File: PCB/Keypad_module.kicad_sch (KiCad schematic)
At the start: 67 parts, among them SW83 SW_Push, SW84 SW_Push, SW85 SW_Push, SW86 SW_Push, SW87 SW_Push, SW88 SW_Push, SW89 SW_Push, SW90 SW_Push, SW91 SW_Push, SW92 SW_Push, SW93 SW_Push, SW94 SW_Push, SW95 SW_Push, SW96 SW_Push, SW97 SW_Push, SW98 SW_Push, SW99 SW_Push, U5 XIAO-nRF52840-SMD, U6 MCP23017_ML

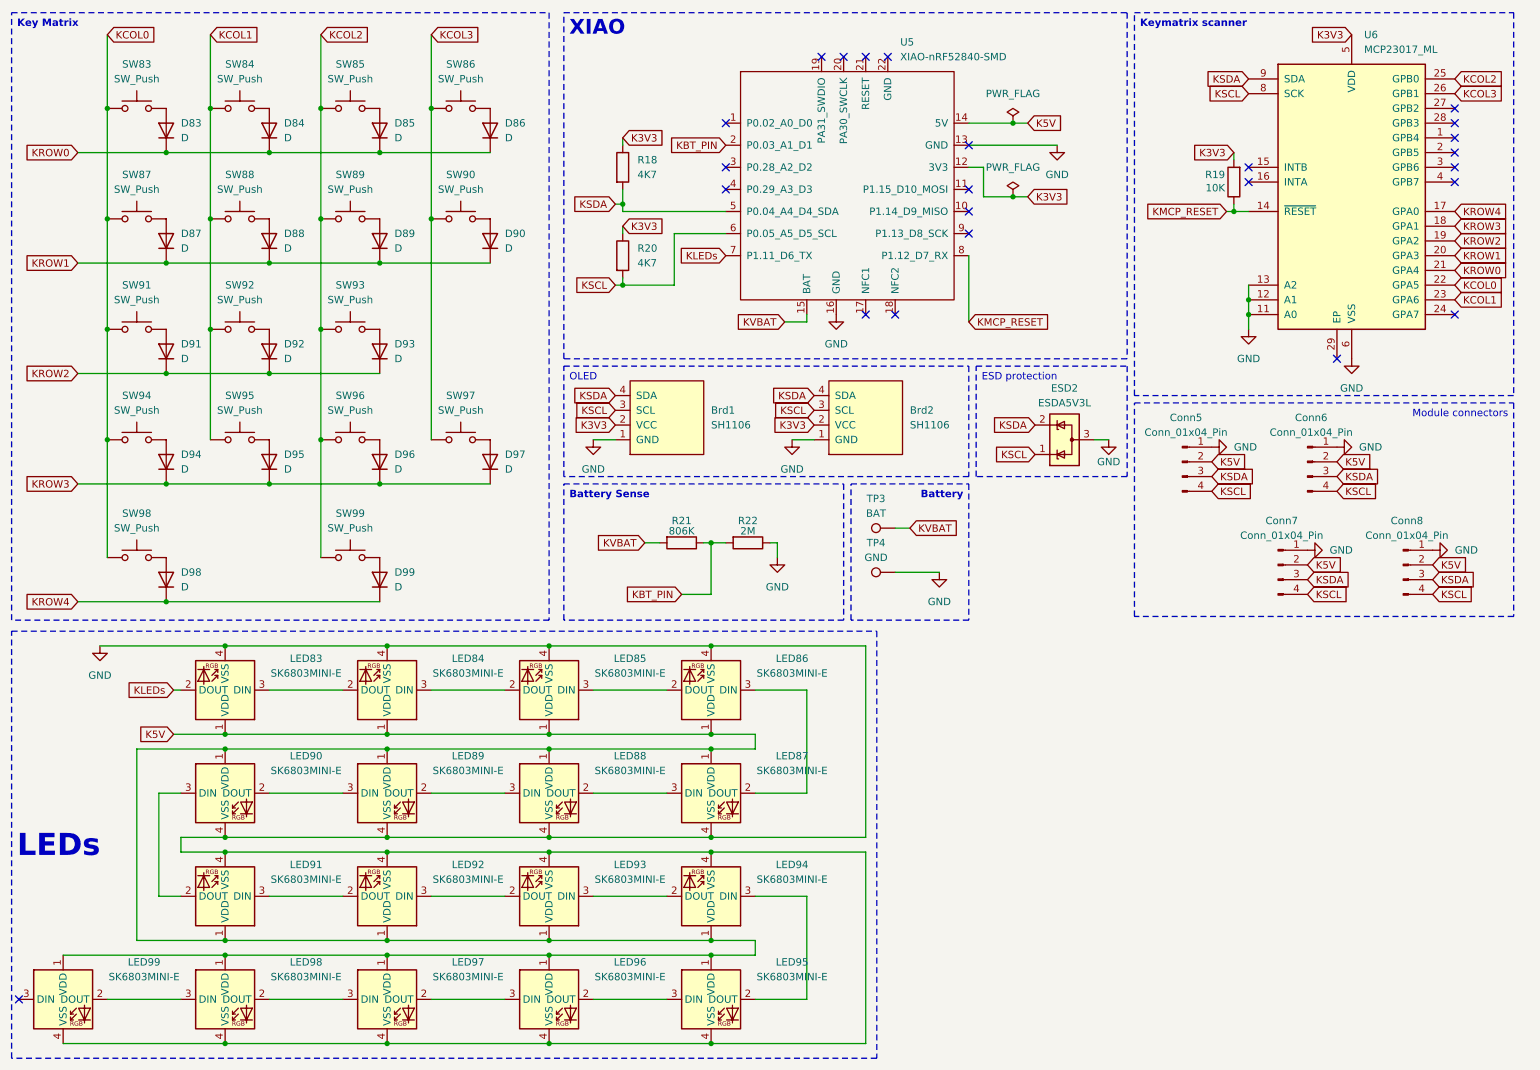
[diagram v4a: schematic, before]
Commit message: Update: schematic and PCB
Replaced the MT3608 module with a custom circuit for it.
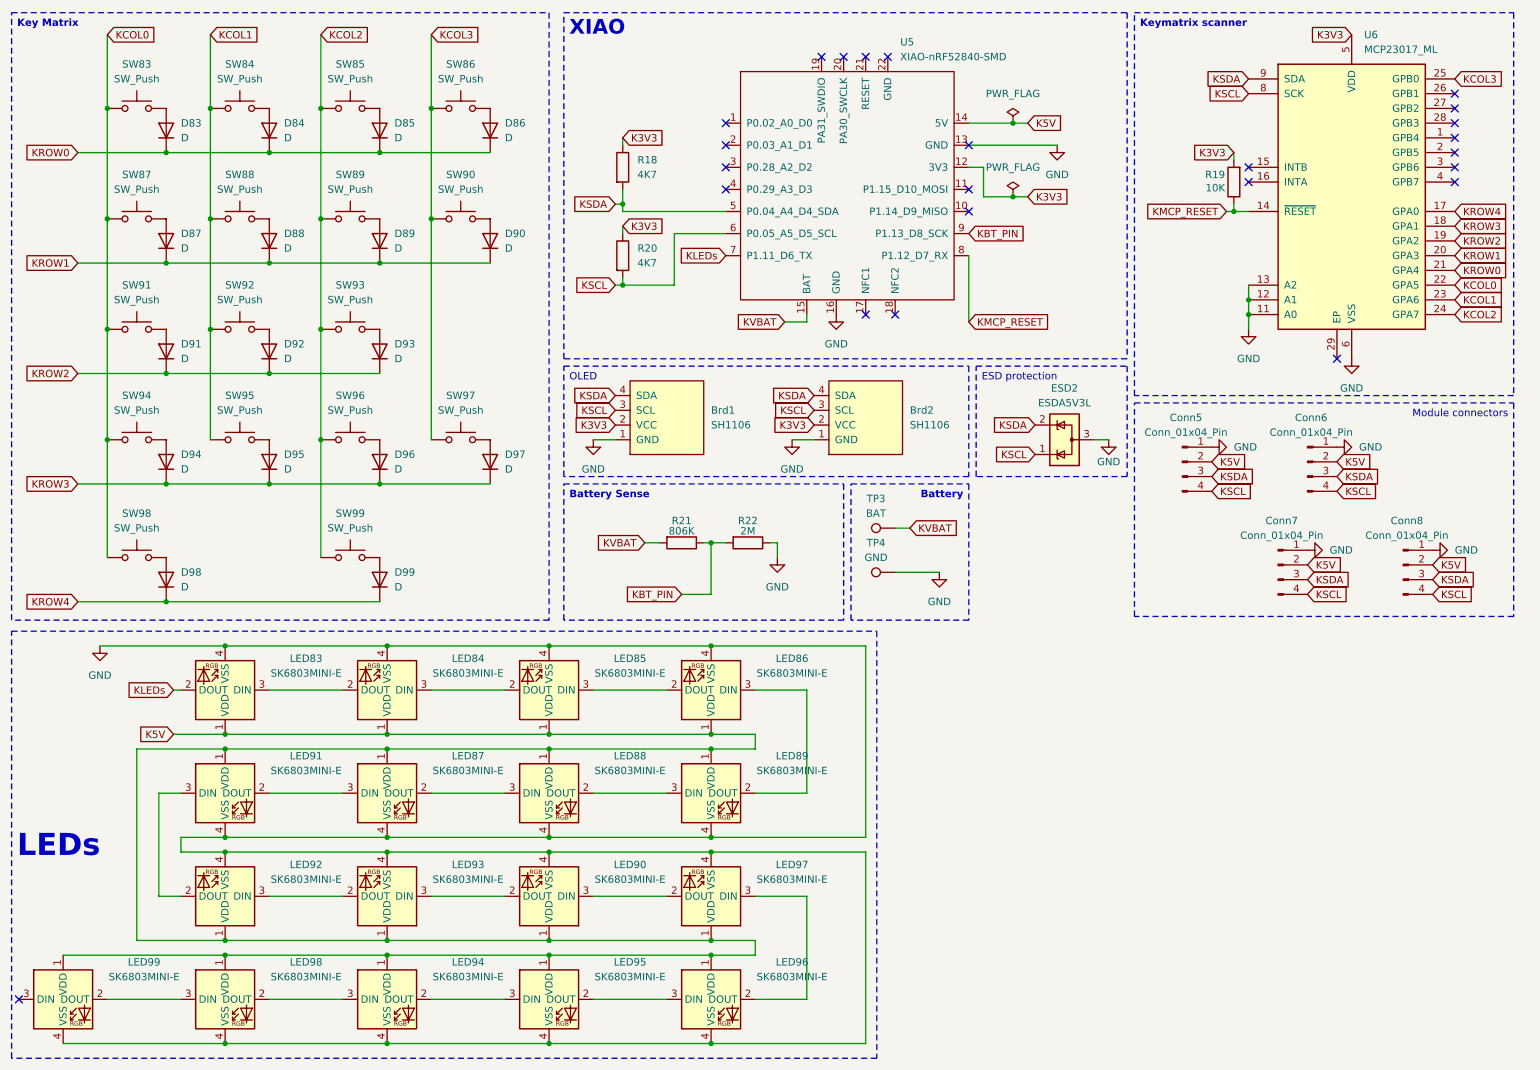
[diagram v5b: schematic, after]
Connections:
- net KBT_PIN: now also U5.9 (P1.13_D8_SCK); no longer U5.2 (P0.03_A1_D1)
- net KCOL2: now also U6.24 (GPA7); no longer U6.25 (GPB0)
- net KCOL3: now also U6.25 (GPB0); no longer U6.26 (GPB1)
- net at LED97.2 (DOUT): now also LED90.3 (DIN); no longer LED96.3 (DIN)
- net at LED97.3 (DIN): now also LED96.2 (DOUT); no longer LED98.2 (DOUT)
- net at LED86.3 (DIN): now also LED89.2 (DOUT); no longer LED87.2 (DOUT)
- net at LED91.2 (DOUT): now also LED87.3 (DIN); no longer LED90.3 (DIN)
- net at LED95.3 (DIN): now also LED94.2 (DOUT); no longer LED96.2 (DOUT)
- net at LED95.2 (DOUT): now also LED96.3 (DIN); no longer LED94.3 (DIN)
- net at LED88.3 (DIN): now also LED87.2 (DOUT); no longer LED89.2 (DOUT)
- net at LED89.3 (DIN): now also LED88.2 (DOUT); no longer LED90.2 (DOUT)
- net at LED93.3 (DIN): now also LED90.2 (DOUT); no longer LED94.2 (DOUT)
- new net: LED94.3 (DIN), LED98.2 (DOUT)
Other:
- moved on the sheet: LED87, LED89, LED90, LED91, LED92, LED93, LED94, LED95, LED96, LED97

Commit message: Update: change footprint to V1V2, update 3D models, Add rotary encoder and 128x32 OLED, Remove second 128x64 OLED
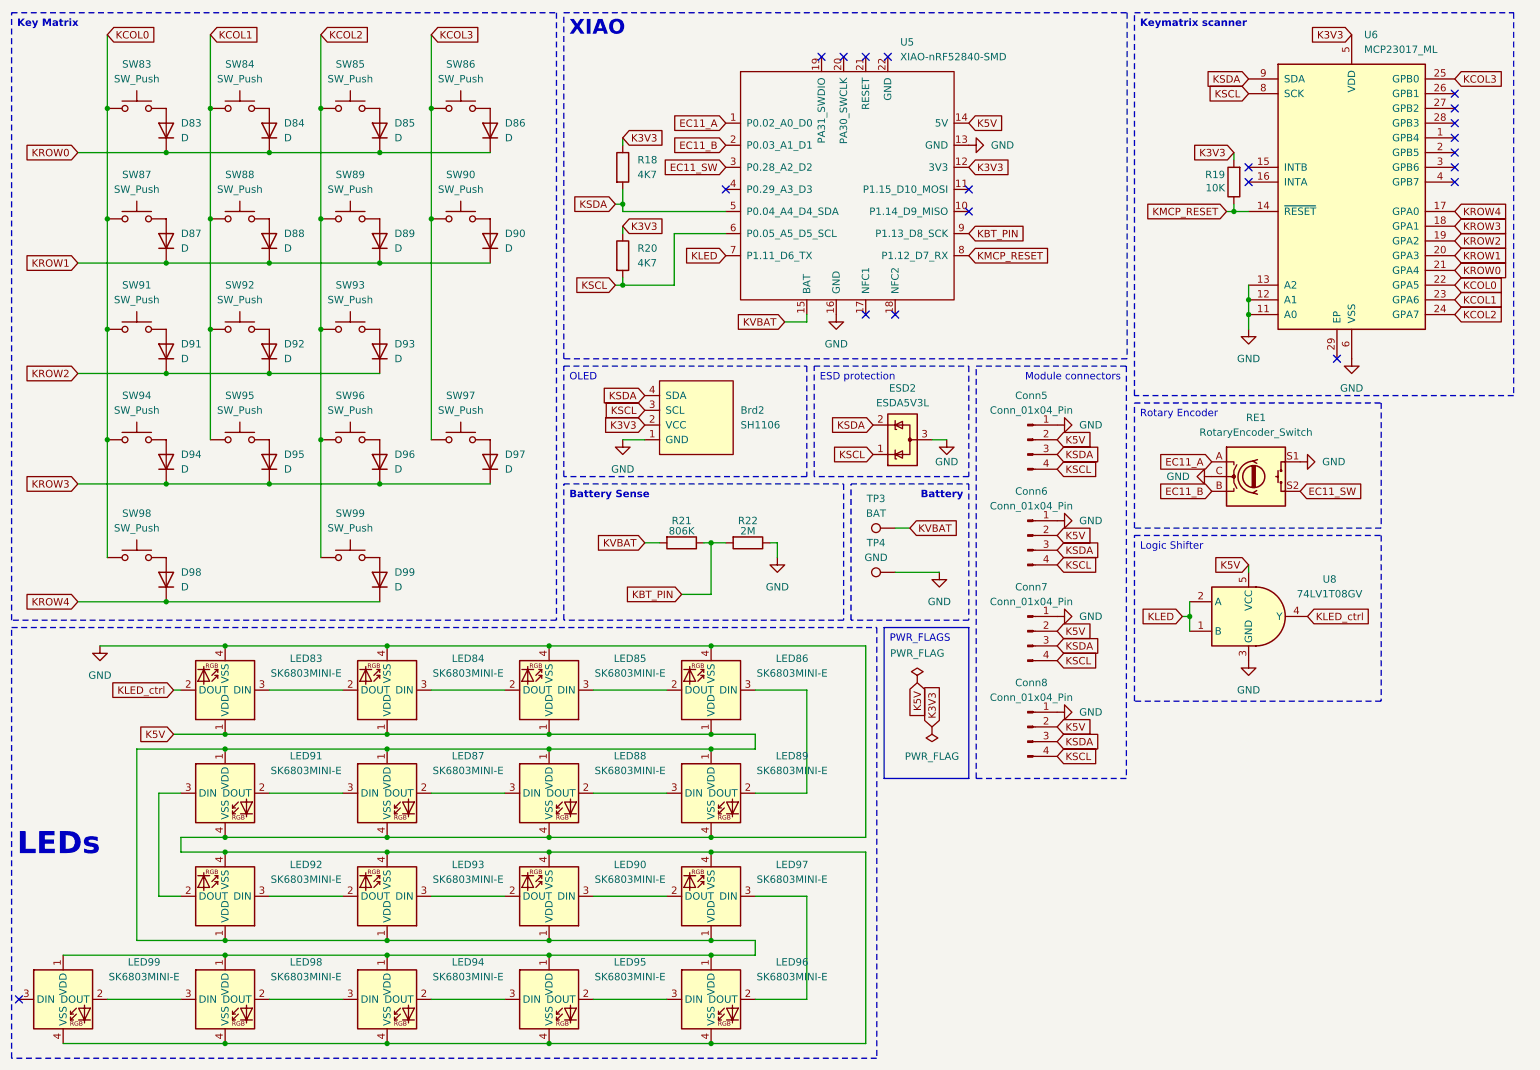
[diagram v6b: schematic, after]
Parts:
- removed Brd1: SH1106, Footprints:128x64OLED, symbol SSD1306-128x64_OLED:SSD1306
- added RE1: RotaryEncoder_Switch, Rotary_Encoder:RotaryEncoder_Alps_EC11E-Switch_Vertical_H20mm_CircularMountingHoles, symbol Device:RotaryEncoder_Switch
- added U8: 74LV1T08GV, Package_TO_SOT_SMD:SC-74A-5_1.55x2.9mm_P0.95mm, symbol 74xx:74LV1T08GV
- SW83, SW84, SW85, SW86, SW87, SW88, SW89, SW91, SW92, SW93, SW94, SW95, SW96, SW99: footprint Footprints:Kailh_choc_HS_V2_1u -> Footprints:Kailh_choc_HS_V1V2_1u
- SW90, SW97: footprint Footprints:Kailh_choc_HS_V2_2u_90deg -> Footprints:Kailh_choc_HS_V1V2_2u_90deg
- SW98: footprint Footprints:Kailh_choc_HS_V2_2u -> Footprints:Kailh_choc_HS_V1V2_2u
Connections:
- net GND: now also RE1.C, RE1.S1, U8.3 (GND)
- net K5V: now also U8.5 (VCC)
- net EC11_A: now reaches U5.1 (P0.02_A0_D0)
- net EC11_A: now also RE1.A
- net EC11_B: now reaches U5.2 (P0.03_A1_D1)
- net EC11_B: now also RE1.B
- net EC11_SW: now reaches U5.3 (P0.28_A2_D2)
- net EC11_SW: now also RE1.S2
- net KLEDs renamed KLED
- net KLED: now also U8.1 (B), U8.2 (A); no longer LED83.2 (DOUT)
- new net KLED_ctrl: LED83.2 (DOUT), U8.4 (Y)
- no-connect marks 24 -> 20
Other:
- moved on the sheet: Brd2, Conn5, Conn6, Conn7, Conn8, ESD2

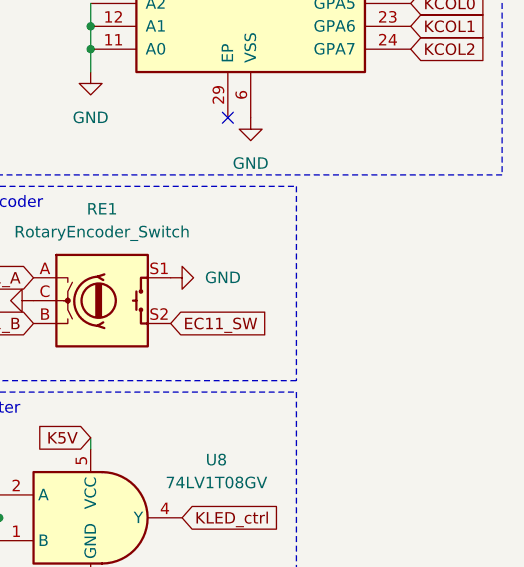
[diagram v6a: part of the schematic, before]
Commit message: Update: Changed keyswitch footprints to HS MX switches
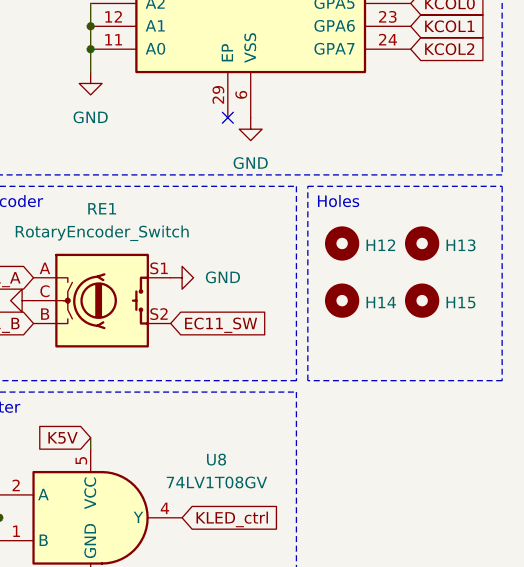
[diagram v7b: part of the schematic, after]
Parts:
- added H12, H13, H14, H15: MountingHole, MountingHole:MountingHole_2.2mm_M2, symbol Mechanical:MountingHole
- Conn5, Conn7: footprint Connector_PinHeader_2.54mm:PinHeader_1x04_P2.54mm_Vertical -> Footprints:Pogopin_Conn_1x4_Female
- Conn6, Conn8: footprint Connector_PinHeader_2.54mm:PinHeader_1x04_P2.54mm_Vertical -> Footprints:Pogopin_Conn_1x4_Male
- SW83, SW84, SW85, SW86, SW87, SW88, SW89, SW91, SW92, SW93, SW94, SW95, SW96, SW99: footprint Footprints:Kailh_choc_HS_V1V2_1u -> Footprints:MX_HS_1u
- SW90, SW97: footprint Footprints:Kailh_choc_HS_V1V2_2u_90deg -> Footprints:MX_HS_2u_90deg
- SW98: footprint Footprints:Kailh_choc_HS_V1V2_2u -> Footprints:MX_HS_2u

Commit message: Init: Keyboard Case
Development only
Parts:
- H12, H13, H14, H15: footprint MountingHole:MountingHole_2.2mm_M2 -> MountingHole:MountingHole_3.2mm_M3
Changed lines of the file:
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@@
 			)
 		)
-		(property "Footprint" "MountingHole:MountingHole_2.2mm_M2"
+		(property "Footprint" "MountingHole:MountingHole_3.2mm_M3"
 			(at 266.7 95.25 0)
 			(effects
@@
 			)
 		)
-		(property "Footprint" "MountingHole:MountingHole_2.2mm_M2"
+		(property "Footprint" "MountingHole:MountingHole_3.2mm_M3"
 			(at 266.7 88.9 0)
 			(effects
@@
 			)
 		)
-		(property "Footprint" "MountingHole:MountingHole_2.2mm_M2"
+		(property "Footprint" "MountingHole:MountingHole_3.2mm_M3"
 			(at 257.81 95.25 0)
 			(effects
@@
 			)
 		)
-		(property "Footprint" "MountingHole:MountingHole_2.2mm_M2"
+		(property "Footprint" "MountingHole:MountingHole_3.2mm_M3"
 			(at 257.81 88.9 0)
 			(effects
